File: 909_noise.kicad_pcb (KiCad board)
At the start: 2 copper layers, 30 x 20 mm, 20 parts, among them J1 1x2 Header, J2 1x3 Header, J3 3220-10-0300-00, SW1 PTS645SM43SMTR92 LFS, U1 STM32G030J6M6, U2 L78L33ABUTR, U3 TLV7211AIDBVR

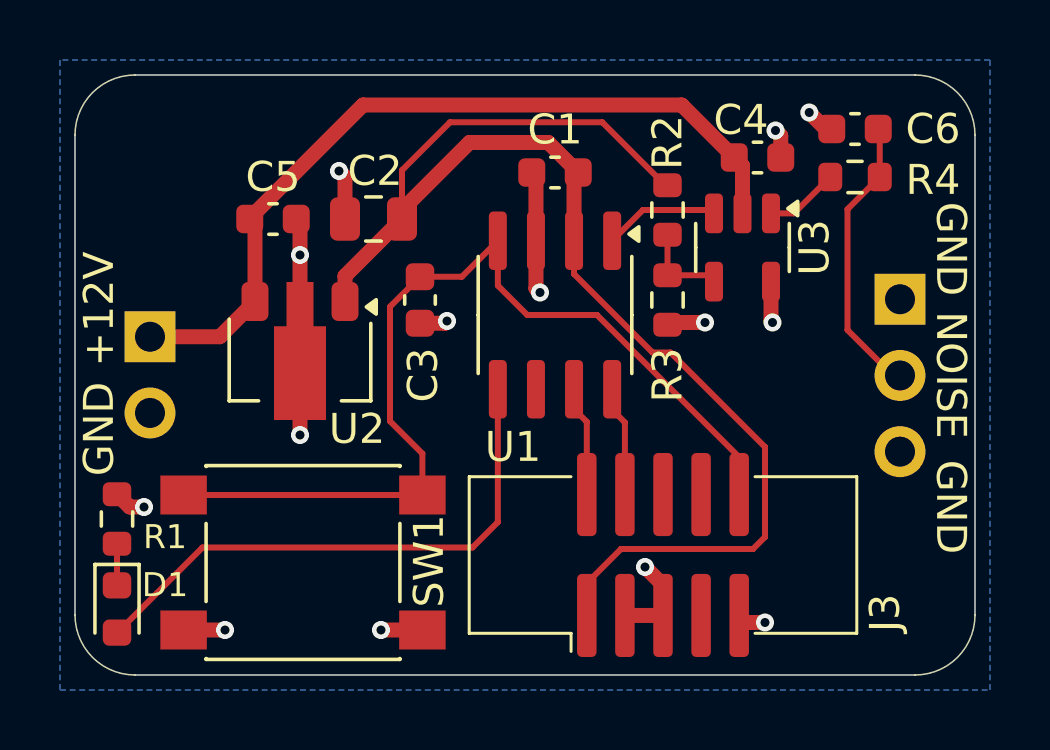
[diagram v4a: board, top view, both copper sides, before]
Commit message: routed with single-supply +12V on opamp
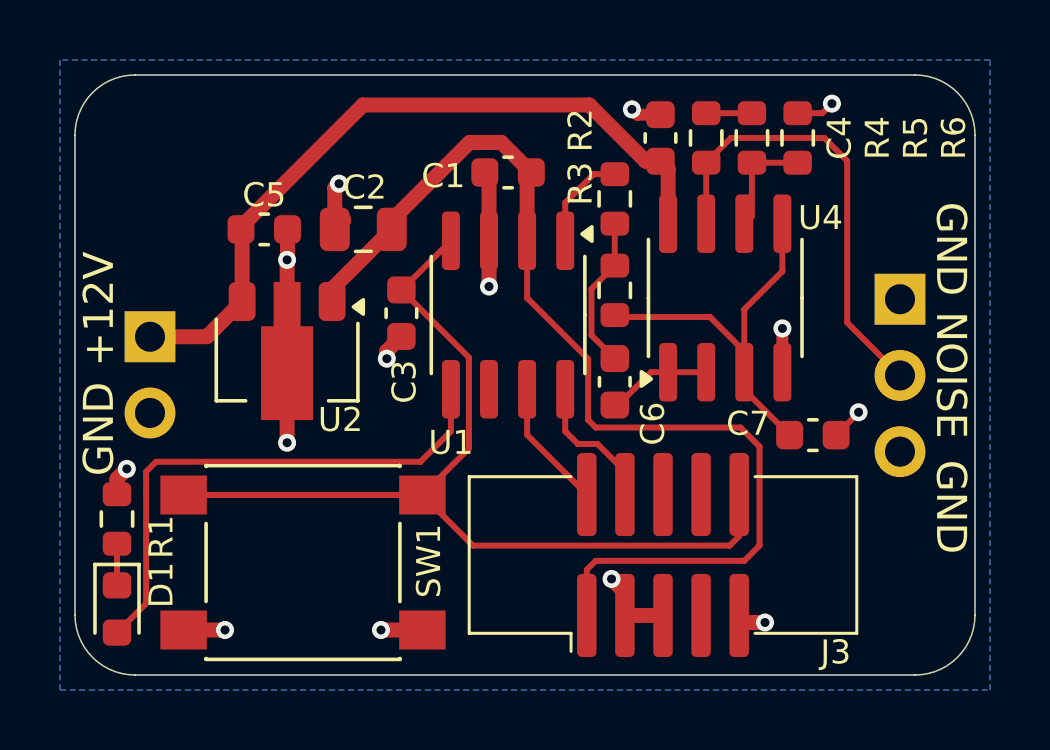
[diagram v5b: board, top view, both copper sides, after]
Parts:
- removed U3: TLV7211AIDBVR, Package_TO_SOT_SMD:SOT-23-5
- added C7: 470p, Capacitor_SMD:C_0603_1608Metric, F.Cu at (69.6, 32.0)
- added R5: 10k, Resistor_SMD:R_0603_1608Metric, F.Cu at (67.6, 22.1)
- added R6: 10k, Resistor_SMD:R_0603_1608Metric, F.Cu at (69.1, 22.1)
- added U4: NE5532, Package_SO:SOIC-8_3.9x4.9mm_P1.27mm, F.Cu at (66.7, 27.4)
- C6: value 100n -> 470p
- R2, R3: value 10k -> 3.4k
- R4: value 15 -> 10k
- moved C6 11.6 mm to (63.0, 30.2), turned to -90 degrees
- moved R4 5.13 mm to (66.0, 22.1), turned to 90 degrees
- moved C4 3.30 mm to (64.5, 22.1), turned to -90 degrees
- moved R2 1.80 mm to (63.0, 24.1)
- moved R3 1.79 mm to (63.0, 27.2)
- moved C1 1.56 mm to (59.4, 23.2)
- moved U1 1.56 mm to (59.4, 28.0)
- moved C3 0.76 mm to (55.9, 27.9)
- moved C2 0.49 mm to (54.6, 25.1)
- moved C5 0.45 mm to (51.3, 25.1)
- moved U2 0.43 mm to (52.1, 29.5)
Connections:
- C6 pad 1: GND -> Net-(C6-Pad1)
- C6 pad 2: /noise_12v_filtered -> Net-(U4A--)
- J2 pad 2: /noise_12v_filtered -> /noise_12v
- R2 pad 1: +3.3V -> /noise_3v3
- R2 pad 2: Net-(U3--) -> Net-(C6-Pad1)
- R3 pad 1: Net-(U3--) -> Net-(C6-Pad1)
- R3 pad 2: GND -> Net-(U4A-+)
- R4 pad 2: /noise_12v_filtered -> Net-(R4-Pad2)
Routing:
- net Net-(U4A-+): track 0.00 -> 13.0 mm
- net /noise_12v: track 2.48 -> 15.3 mm
- net +3.3V: track 45.9 -> 35.8 mm
- net /noise_12v_filtered: track 9.54 -> 0.00 mm
- net Net-(C6-Pad1): track 0.00 -> 5.14 mm
- net Net-(U4B--): track 0.00 -> 3.66 mm
- net Net-(U4A--): track 0.00 -> 3.50 mm
- net Net-(U3--): track 2.99 -> 0.00 mm
- net +12V: track 27.2 -> 24.7 mm
- net Net-(R4-Pad2): track 0.00 -> 1.52 mm
- net /swclk: track 3.69 -> 4.72 mm
- net /~{reset}: track 32.3 -> 31.5 mm
- net Net-(D1-A): track 18.7 -> 17.9 mm
- net /swdio: track 3.69 -> 4.33 mm
- net /noise_3v3: track 3.87 -> 3.31 mm

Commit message: add -12V to opamp
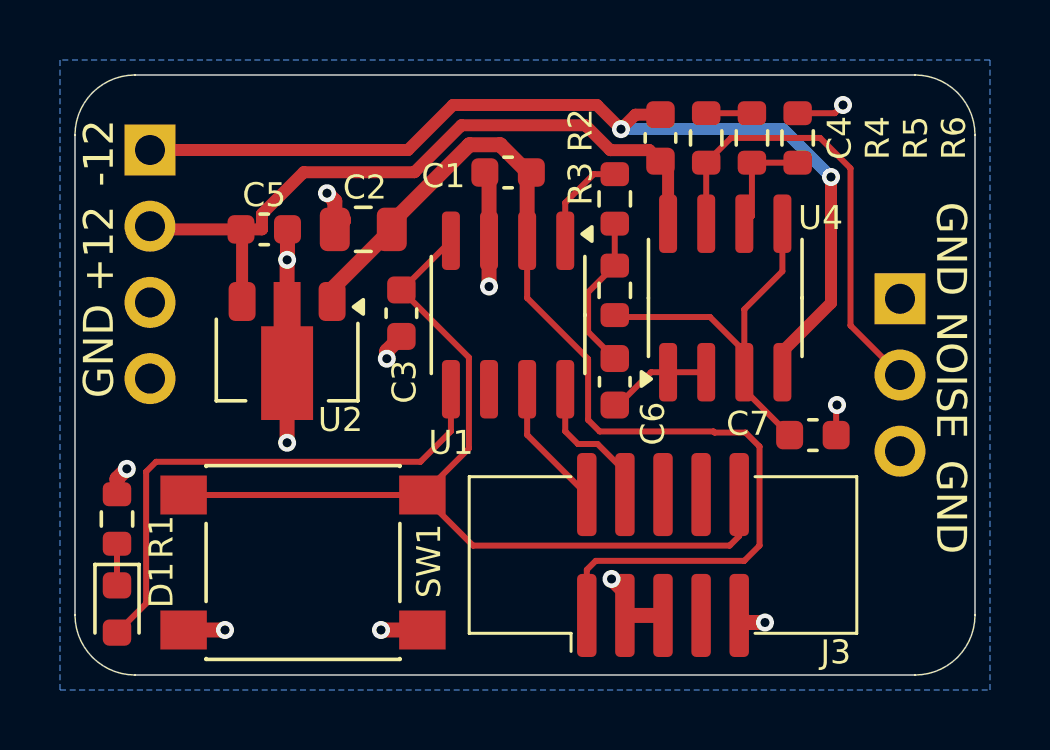
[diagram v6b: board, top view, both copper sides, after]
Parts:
- J1: value 1x2 Header -> 1x4 Header; footprint Connector_PinHeader_2.54mm:PinHeader_1x02_P2.54mm_Vertical -> Connector_PinHeader_2.54mm:PinHeader_1x04_P2.54mm_Vertical
- moved J1 6.23 mm to (47.5, 22.5)
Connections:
- C4 pad 1: GND -> -12V
- J1 pad 1: +12V -> -12V
- J1 pad 2: GND -> +12V
- U4 pad 4: GND -> -12V
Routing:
- net -12V: track 0.00 -> 33.0 mm, vias 0 -> 2
- net GND: track 26.2 -> 23.7 mm, vias 14 -> 12
- net +12V: track 24.7 -> 23.9 mm
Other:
- board text added: "+12"
- board text added: "-12"
- board text removed: "+12V"
